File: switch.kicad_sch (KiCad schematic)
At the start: 6 parts, among them Q1 Q_Photo_NPN

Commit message: updated pcb
M  optical-keyboard.kicad_pcb
M  optical-keyboard.kicad_pro
M  optical-keyboard.kicad_sch
M  placefp.py
M  switch.kicad_sch
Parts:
- renumbered D1 to D17, N1 to N17, Q1 to Q17, RL1 to RL17, RP1 to RP17, S1 to S17
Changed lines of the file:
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@@
   (symbol (lib_id "OpticalParts:IR_LED") (at 116.84 100.33 90)
     (in_bom yes) (on_board yes) (fields_autoplaced)
-    (property "Reference" "D1" (id 0) (at 119.761 101.0828 90)
+    (property "Reference" "D17" (id 0) (at 119.761 101.0828 90)
       (effects (font (size 1.27 1.27)) (justify right))
     )
@@
   (symbol (lib_id "OpticalParts:Q_Photo_NPN") (at 143.51 99.06 0)
     (in_bom yes) (on_board yes) (fields_autoplaced)
-    (property "Reference" "Q1" (id 0) (at 148.3614 97.476 0)
+    (property "Reference" "Q17" (id 0) (at 148.3614 97.476 0)
       (effects (font (size 1.27 1.27)) (justify left))
     )
@@
   (symbol (lib_id "OpticalParts:Gateron_Optical") (at 133.35 59.69 0)
     (in_bom yes) (on_board yes) (fields_autoplaced)
-    (property "Reference" "S1" (id 0) (at 136.6012 58.8553 0)
+    (property "Reference" "S17" (id 0) (at 136.6012 58.8553 0)
       (effects (font (size 1.27 1.27)) (justify left))
     )
@@
   (symbol (lib_id "OpticalParts:R_PT") (at 146.05 83.82 0)
     (in_bom yes) (on_board yes) (fields_autoplaced)
-    (property "Reference" "RP1" (id 0) (at 147.828 82.9853 0)
+    (property "Reference" "RP17" (id 0) (at 147.828 82.9853 0)
       (effects (font (size 1.27 1.27)) (justify left))
     )
@@
   (symbol (lib_id "OpticalParts:Diode1N4148WSSod323") (at 158.75 90.17 180)
     (in_bom yes) (on_board yes) (fields_autoplaced)
-    (property "Reference" "N1" (id 0) (at 158.75 85.2002 0))
+    (property "Reference" "N17" (id 0) (at 158.75 85.2002 0))
     (property "Value" "Diode1N4148WSSod323" (id 1) (at 158.75 87.7371 0))
     (property "Footprint" "Diode_SMD:D_SOD-323_HandSoldering" (id 2) (at 158.75 85.725 0)
@@
   (symbol (lib_id "OpticalParts:R_Led") (at 116.84 83.82 0)
     (in_bom yes) (on_board yes) (fields_autoplaced)
-    (property "Reference" "RL1" (id 0) (at 118.618 82.9853 0)
+    (property "Reference" "RL17" (id 0) (at 118.618 82.9853 0)
       (effects (font (size 1.27 1.27)) (justify left))
     )
@@
   (symbol (lib_id "power:GND") (at 116.84 119.38 0)
     (in_bom yes) (on_board yes) (fields_autoplaced)
-    (property "Reference" "#PWR04" (id 0) (at 116.84 125.73 0)
+    (property "Reference" "#PWR078" (id 0) (at 116.84 125.73 0)
       (effects (font (size 1.27 1.27)) hide)
     )

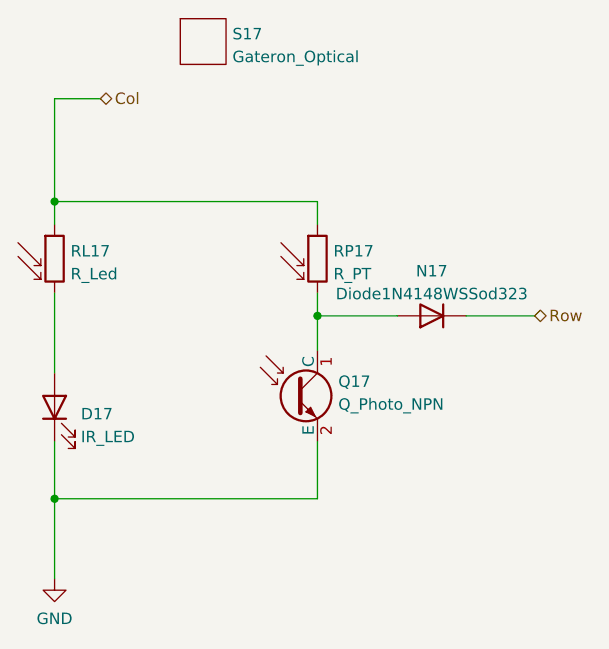
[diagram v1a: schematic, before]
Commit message: update schematic
M  optical-keyboard.kicad_sch
M  switch.kicad_sch
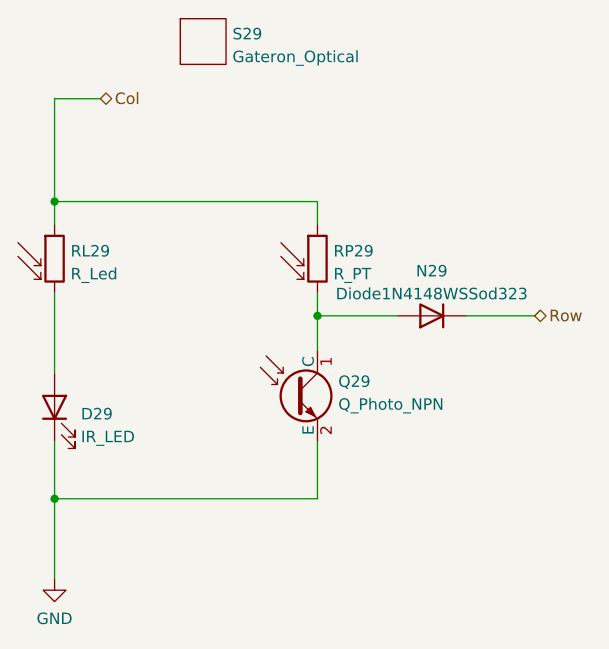
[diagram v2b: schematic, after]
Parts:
- renumbered D17 to D29, N17 to N29, Q17 to Q29, RL17 to RL29, RP17 to RP29, S17 to S29
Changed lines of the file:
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@@
   (symbol (lib_id "OpticalParts:IR_LED") (at 116.84 100.33 90)
     (in_bom yes) (on_board yes) (fields_autoplaced)
-    (property "Reference" "D17" (id 0) (at 119.761 101.0828 90)
+    (property "Reference" "D29" (id 0) (at 119.761 101.0828 90)
       (effects (font (size 1.27 1.27)) (justify right))
     )
@@
   (symbol (lib_id "OpticalParts:Q_Photo_NPN") (at 143.51 99.06 0)
     (in_bom yes) (on_board yes) (fields_autoplaced)
-    (property "Reference" "Q17" (id 0) (at 148.3614 97.476 0)
+    (property "Reference" "Q29" (id 0) (at 148.3614 97.476 0)
       (effects (font (size 1.27 1.27)) (justify left))
     )
@@
   (symbol (lib_id "OpticalParts:Gateron_Optical") (at 133.35 59.69 0)
     (in_bom yes) (on_board yes) (fields_autoplaced)
-    (property "Reference" "S17" (id 0) (at 136.6012 58.8553 0)
+    (property "Reference" "S29" (id 0) (at 136.6012 58.8553 0)
       (effects (font (size 1.27 1.27)) (justify left))
     )
@@
   (symbol (lib_id "OpticalParts:R_PT") (at 146.05 83.82 0)
     (in_bom yes) (on_board yes) (fields_autoplaced)
-    (property "Reference" "RP17" (id 0) (at 147.828 82.9853 0)
+    (property "Reference" "RP29" (id 0) (at 147.828 82.9853 0)
       (effects (font (size 1.27 1.27)) (justify left))
     )
@@
   (symbol (lib_id "OpticalParts:Diode1N4148WSSod323") (at 158.75 90.17 180)
     (in_bom yes) (on_board yes) (fields_autoplaced)
-    (property "Reference" "N17" (id 0) (at 158.75 85.2002 0))
+    (property "Reference" "N29" (id 0) (at 158.75 85.2002 0))
     (property "Value" "Diode1N4148WSSod323" (id 1) (at 158.75 87.7371 0))
     (property "Footprint" "Diode_SMD:D_SOD-323_HandSoldering" (id 2) (at 158.75 85.725 0)
@@
   (symbol (lib_id "OpticalParts:R_Led") (at 116.84 83.82 0)
     (in_bom yes) (on_board yes) (fields_autoplaced)
-    (property "Reference" "RL17" (id 0) (at 118.618 82.9853 0)
+    (property "Reference" "RL29" (id 0) (at 118.618 82.9853 0)
       (effects (font (size 1.27 1.27)) (justify left))
     )

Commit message: Fixed bug in symbols by removing arrows
M  optical-keyboard.kicad_sch
M  switch.kicad_sch
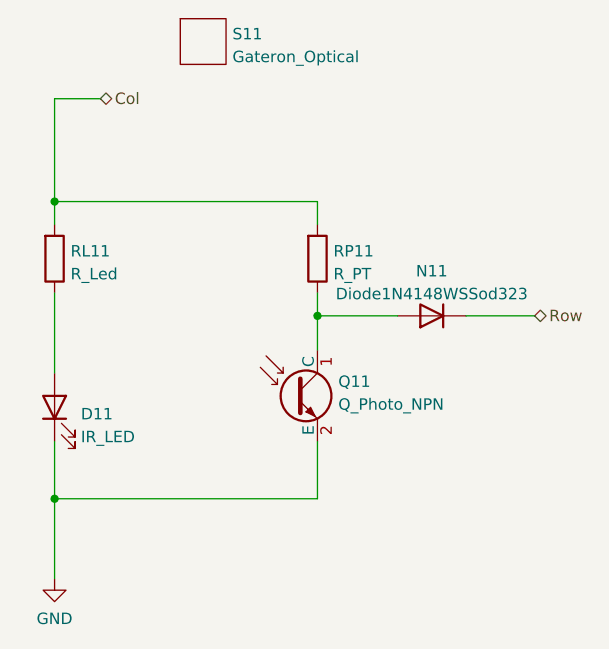
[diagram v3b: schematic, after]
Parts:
- N11: renamed from N29; footprint Diode_SMD:D_SOD-323_HandSoldering -> Diode_SMD:D_SOD-323
- renumbered D29 to D11, Q29 to Q11, RL29 to RL11, RP29 to RP11, S29 to S11
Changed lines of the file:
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@@
   (symbol (lib_id "OpticalParts:IR_LED") (at 116.84 100.33 90)
     (in_bom yes) (on_board yes) (fields_autoplaced)
-    (property "Reference" "D29" (id 0) (at 119.761 101.0828 90)
+    (property "Reference" "D11" (id 0) (at 119.761 101.0828 90)
       (effects (font (size 1.27 1.27)) (justify right))
     )
@@
   (symbol (lib_id "OpticalParts:Q_Photo_NPN") (at 143.51 99.06 0)
     (in_bom yes) (on_board yes) (fields_autoplaced)
-    (property "Reference" "Q29" (id 0) (at 148.3614 97.476 0)
+    (property "Reference" "Q11" (id 0) (at 148.3614 97.476 0)
       (effects (font (size 1.27 1.27)) (justify left))
     )
@@
   (symbol (lib_id "OpticalParts:Gateron_Optical") (at 133.35 59.69 0)
     (in_bom yes) (on_board yes) (fields_autoplaced)
-    (property "Reference" "S29" (id 0) (at 136.6012 58.8553 0)
+    (property "Reference" "S11" (id 0) (at 136.6012 58.8553 0)
       (effects (font (size 1.27 1.27)) (justify left))
     )
@@
   (symbol (lib_id "OpticalParts:R_PT") (at 146.05 83.82 0)
     (in_bom yes) (on_board yes) (fields_autoplaced)
-    (property "Reference" "RP29" (id 0) (at 147.828 82.9853 0)
+    (property "Reference" "RP11" (id 0) (at 147.828 82.9853 0)
       (effects (font (size 1.27 1.27)) (justify left))
     )
@@
   (symbol (lib_id "OpticalParts:Diode1N4148WSSod323") (at 158.75 90.17 180)
     (in_bom yes) (on_board yes) (fields_autoplaced)
-    (property "Reference" "N29" (id 0) (at 158.75 85.2002 0))
+    (property "Reference" "N11" (id 0) (at 158.75 85.2002 0))
     (property "Value" "Diode1N4148WSSod323" (id 1) (at 158.75 87.7371 0))
-    (property "Footprint" "Diode_SMD:D_SOD-323_HandSoldering" (id 2) (at 158.75 85.725 0)
+    (property "Footprint" "Diode_SMD:D_SOD-323" (id 2) (at 158.75 85.725 0)
       (effects (font (size 1.27 1.27)) hide)
     )
@@
   (symbol (lib_id "OpticalParts:R_Led") (at 116.84 83.82 0)
     (in_bom yes) (on_board yes) (fields_autoplaced)
-    (property "Reference" "RL29" (id 0) (at 118.618 82.9853 0)
+    (property "Reference" "RL11" (id 0) (at 118.618 82.9853 0)
       (effects (font (size 1.27 1.27)) (justify left))
     )
@@
   (symbol (lib_id "power:GND") (at 116.84 119.38 0)
     (in_bom yes) (on_board yes) (fields_autoplaced)
-    (property "Reference" "#PWR078" (id 0) (at 116.84 125.73 0)
+    (property "Reference" "#PWR014" (id 0) (at 116.84 125.73 0)
       (effects (font (size 1.27 1.27)) hide)
     )

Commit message: Add separate power source for PTs
Sharing input pin b/w pt and led requires a diode, and diode
slows down the response time of pt considerably

M  optical-keyboard.kicad_pcb
M  optical-keyboard.kicad_prl
M  optical-keyboard.kicad_sch
M  placefp.py
M  switch.kicad_sch
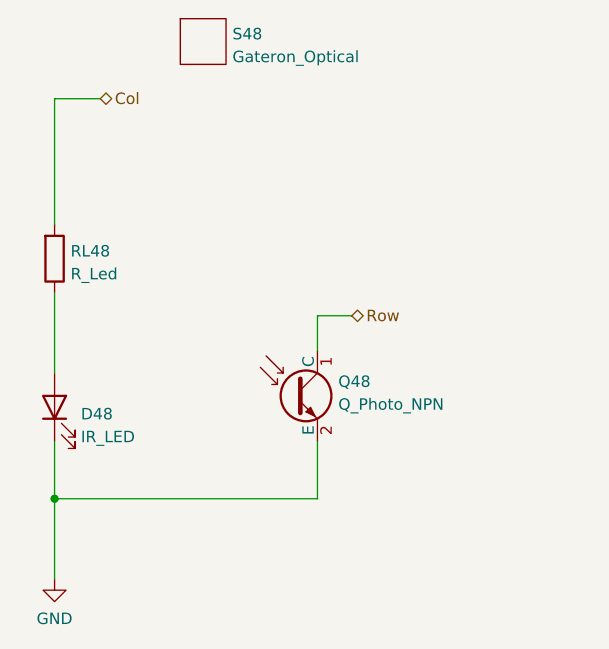
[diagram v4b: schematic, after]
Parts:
- removed N11: Diode1N4148WSSod323, Diode_SMD:D_SOD-323, symbol OpticalParts:Diode1N4148WSSod323
- removed RP11: R_PT, Resistor_SMD:R_0805_2012Metric, symbol OpticalParts:R_PT
- renumbered D11 to D48, Q11 to Q48, RL11 to RL48, S11 to S48
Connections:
- net Row: now also Q48.1 (C)
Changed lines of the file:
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@@
   (junction (at 116.84 110.49) (diameter 0) (color 0 0 0 0)
   )
-  (junction (at 116.84 77.47) (diameter 0) (color 0 0 0 0)
-  )
-  (junction (at 146.05 90.17) (diameter 0) (color 0 0 0 0)
-  )
-  (wire (pts (xy 146.05 77.47) (xy 116.84 77.47))
-    (stroke (width 0) (type default) (color 0 0 0 0))
-  )
   (wire (pts (xy 146.05 104.14) (xy 146.05 110.49))
-    (stroke (width 0) (type default) (color 0 0 0 0))
-  )
-  (wire (pts (xy 146.05 80.01) (xy 146.05 77.47))
     (stroke (width 0) (type default) (color 0 0 0 0))
   )
@@
     (stroke (width 0) (type default) (color 0 0 0 0))
   )
-  (wire (pts (xy 116.84 66.04) (xy 116.84 77.47))
+  (wire (pts (xy 116.84 66.04) (xy 116.84 80.01))
     (stroke (width 0) (type default) (color 0 0 0 0))
   )
-  (wire (pts (xy 146.05 90.17) (xy 154.94 90.17))
+  (wire (pts (xy 146.05 90.17) (xy 149.86 90.17))
     (stroke (width 0) (type default) (color 0 0 0 0))
   )
@@
   )
   (wire (pts (xy 116.84 66.04) (xy 121.92 66.04))
-    (stroke (width 0) (type default) (color 0 0 0 0))
-  )
-  (wire (pts (xy 116.84 77.47) (xy 116.84 80.01))
     (stroke (width 0) (type default) (color 0 0 0 0))
   )
@@
     (stroke (width 0) (type default) (color 0 0 0 0))
   )
-  (wire (pts (xy 146.05 87.63) (xy 146.05 90.17))
-    (stroke (width 0) (type default) (color 0 0 0 0))
-  )
-  (wire (pts (xy 162.56 90.17) (xy 170.18 90.17))
-    (stroke (width 0) (type default) (color 0 0 0 0))
-  )
   (hierarchical_label "Col" (shape bidirectional) (at 121.92 66.04 0)
     (effects (font (size 1.27 1.27)) (justify left))
   )
-  (hierarchical_label "Row" (shape bidirectional) (at 170.18 90.17 0)
+  (hierarchical_label "Row" (shape bidirectional) (at 149.86 90.17 0)
     (effects (font (size 1.27 1.27)) (justify left))
   )
   (symbol (lib_id "OpticalParts:IR_LED") (at 116.84 100.33 90)
     (in_bom yes) (on_board yes) (fields_autoplaced)
-    (property "Reference" "D11" (id 0) (at 119.761 101.0828 90)
+    (property "Reference" "D48" (id 0) (at 119.761 101.0828 90)
       (effects (font (size 1.27 1.27)) (justify right))
     )
@@
   (symbol (lib_id "OpticalParts:Q_Photo_NPN") (at 143.51 99.06 0)
     (in_bom yes) (on_board yes) (fields_autoplaced)
-    (property "Reference" "Q11" (id 0) (at 148.3614 97.476 0)
+    (property "Reference" "Q48" (id 0) (at 148.3614 97.476 0)
       (effects (font (size 1.27 1.27)) (justify left))
     )
@@
   (symbol (lib_id "OpticalParts:Gateron_Optical") (at 133.35 59.69 0)
     (in_bom yes) (on_board yes) (fields_autoplaced)
-    (property "Reference" "S11" (id 0) (at 136.6012 58.8553 0)
+    (property "Reference" "S48" (id 0) (at 136.6012 58.8553 0)
       (effects (font (size 1.27 1.27)) (justify left))
     )
@@
     )
   )
-  (symbol (lib_id "OpticalParts:R_PT") (at 146.05 83.82 0)
-    (in_bom yes) (on_board yes) (fields_autoplaced)
-    (property "Reference" "RP11" (id 0) (at 147.828 82.9853 0)
-      (effects (font (size 1.27 1.27)) (justify left))
-    )
-    (property "Value" "R_PT" (id 1) (at 147.828 85.5222 0)
-      (effects (font (size 1.27 1.27)) (justify left))
-    )
-    (property "Footprint" "Resistor_SMD:R_0805_2012Metric" (id 2) (at 147.32 90.17 90)
-      (effects (font (size 1.27 1.27)) (justify left) hide)
-    )
-    (property "Datasheet" "~" (id 3) (at 146.05 85.09 0)
-      (effects (font (size 1.27 1.27)) hide)
-    )
-    (property "JLC" "0805-2012" (id 4) (at 143.51 87.63 0)
-      (effects (font (size 0.5 0.5)) hide)
-    )
-    (property "LCSC" "C17713" (id 5) (at 149.86 80.01 0)
-      (effects (font (size 0.5 0.5)) hide)
-    )
-    (pin "1")
-    (pin "2")
-  )
-  (symbol (lib_id "OpticalParts:Diode1N4148WSSod323") (at 158.75 90.17 180)
-    (in_bom yes) (on_board yes) (fields_autoplaced)
-    (property "Reference" "N11" (id 0) (at 158.75 85.2002 0))
-    (property "Value" "Diode1N4148WSSod323" (id 1) (at 158.75 87.7371 0))
-    (property "Footprint" "Diode_SMD:D_SOD-323" (id 2) (at 158.75 85.725 0)
-      (effects (font (size 1.27 1.27)) hide)
-    )
-    (property "Datasheet" "https://www.vishay.com/docs/85751/1n4148ws.pdf" (id 3) (at 158.75 90.17 0)
-      (effects (font (size 1.27 1.27)) hide)
-    )
-    (property "LCSC" "C2128" (id 4) (at 158.75 90.17 0)
-      (effects (font (size 1.27 1.27)) hide)
-    )
-    (property "JLC" "SOD-323" (id 5) (at 158.75 90.17 0)
-      (effects (font (size 1.27 1.27)) hide)
-    )
-    (pin "1")
-    (pin "2")
-  )
   (symbol (lib_id "OpticalParts:R_Led") (at 116.84 83.82 0)
     (in_bom yes) (on_board yes) (fields_autoplaced)
-    (property "Reference" "RL11" (id 0) (at 118.618 82.9853 0)
+    (property "Reference" "RL48" (id 0) (at 118.618 82.9853 0)
       (effects (font (size 1.27 1.27)) (justify left))
     )
@@
   (symbol (lib_id "power:GND") (at 116.84 119.38 0)
     (in_bom yes) (on_board yes) (fields_autoplaced)
-    (property "Reference" "#PWR014" (id 0) (at 116.84 125.73 0)
+    (property "Reference" "#PWR078" (id 0) (at 116.84 125.73 0)
       (effects (font (size 1.27 1.27)) hide)
     )
